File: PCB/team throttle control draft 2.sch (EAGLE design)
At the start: 15 parts, among them IC1 ICL7663CPA, IC4 7805T

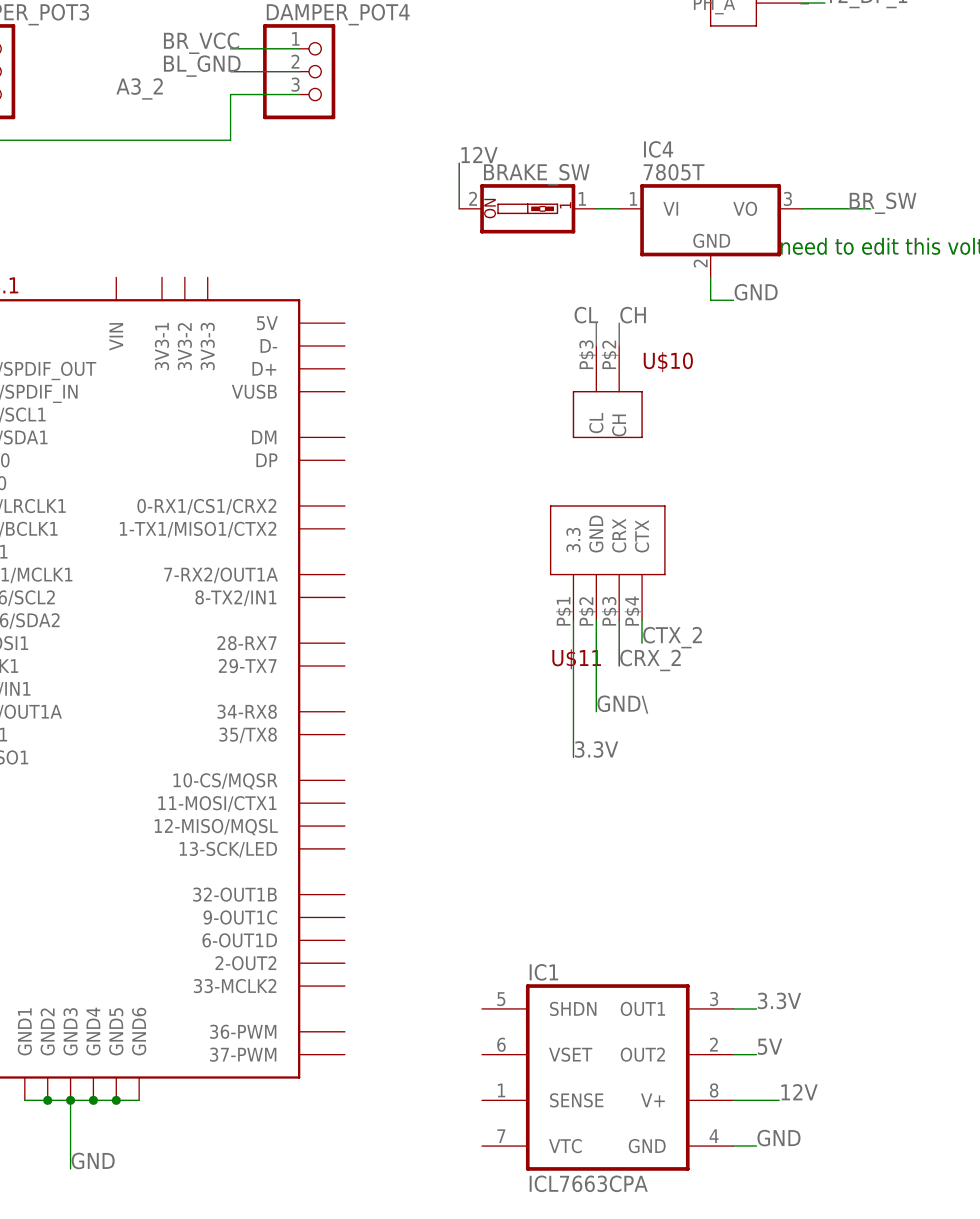
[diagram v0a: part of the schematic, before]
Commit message: Dump car_software's PCB folder into new repository.
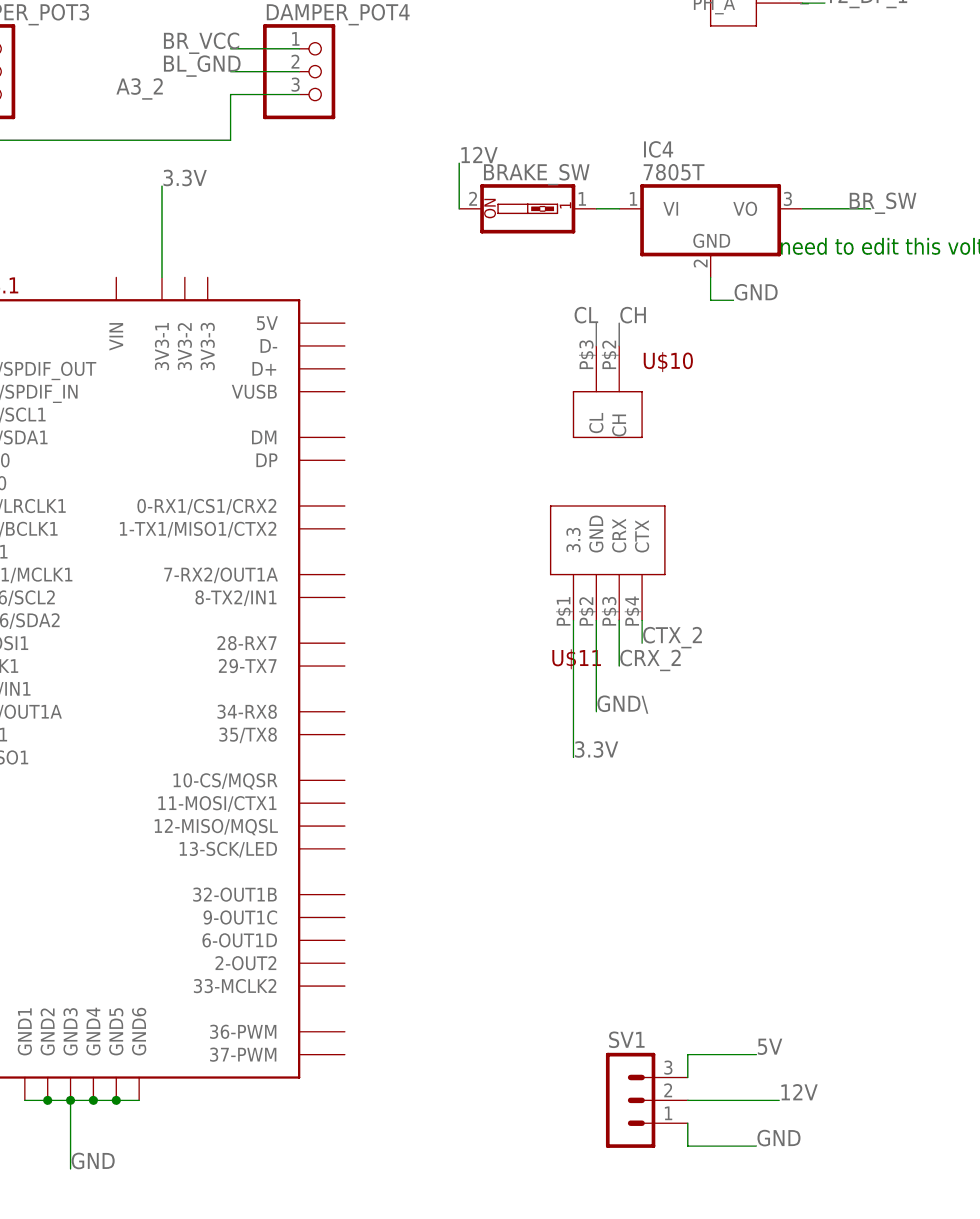
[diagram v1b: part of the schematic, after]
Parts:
- removed IC1: ICL7663CPA, maxim:ICL7663CPA
- added SV1: (no value), con-lstb:MA03-1
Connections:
- net 12V: now also SV1.2; no longer IC1.V+
- net 3.3V: now also U$3.3V3-1; no longer IC1.OUT1
- net 5V: now also SV1.3; no longer IC1.OUT2
- net GND: now also SV1.1; no longer IC1.GND
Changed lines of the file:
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@@
 <?xml version="1.0" encoding="utf-8"?>
 <!DOCTYPE eagle SYSTEM "eagle.dtd">
-<eagle version="7.7.0">
+<eagle version="9.6.2">
 <drawing>
 <settings>
 <setting alwaysvectorfont="no"/>
+<setting keepoldvectorfont="yes"/>
 <setting verticaltext="up"/>
 </settings>
@@
 <layers>
 <layer number="1" name="Top" color="4" fill="1" visible="no" active="no"/>
+<layer number="2" name="Route2" color="1" fill="3" visible="no" active="no"/>
+<layer number="3" name="Route3" color="4" fill="3" visible="no" active="no"/>
+<layer number="4" name="Route4" color="1" fill="4" visible="no" active="no"/>
+<layer number="5" name="Route5" color="4" fill="4" visible="no" active="no"/>
+<layer number="6" name="Route6" color="1" fill="8" visible="no" active="no"/>
+<layer number="7" name="Route7" color="4" fill="8" visible="no" active="no"/>
+<layer number="8" name="Route8" color="1" fill="2" visible="no" active="no"/>
+<layer number="9" name="Route9" color="4" fill="2" visible="no" active="no"/>
+<layer number="10" name="Route10" color="1" fill="7" visible="no" active="no"/>
+<layer number="11" name="Route11" color="4" fill="7" visible="no" active="no"/>
+<layer number="12" name="Route12" color="1" fill="5" visible="no" active="no"/>
+<layer number="13" name="Route13" color="4" fill="5" visible="no" active="no"/>
+<layer number="14" name="Route14" color="1" fill="6" visible="no" active="no"/>
+<layer number="15" name="Route15" color="4" fill="6" visible="no" active="no"/>
 <layer number="16" name="Bottom" color="1" fill="1" visible="no" active="no"/>
 <layer number="17" name="Pads" color="2" fill="1" visible="no" active="no"/>
@@
 <parts>
 <part name="STEERING_ANGLE" library="F-E library custom components" deviceset="ROTARY_ENCODER" device=""/>
-<part name="IC1" library="maxim" deviceset="ICL7663CPA" device=""/>
 <part name="BRAKE_SW" library="special" deviceset="SW_DIP-1" device=""/>
 <part name="DAMPER_POT3" library="adafruit" deviceset="PINHD-1X3" device="CB"/>
@@
 <part name="IC4" library="adafruit" deviceset="78*" device="T" technology="05"/>
 <part name="U$3" library="teensy" deviceset="TEENSY41" device=""/>
+<part name="SV1" library="con-lstb" library_urn="urn:adsk.eagle:library:162" deviceset="MA03-1" device="" package3d_urn="urn:adsk.eagle:package:8339/1"/>
 </parts>
 <sheets>
@@
 <attribute name="NAME" x="129.54" y="147.32" size="1.778" layer="94"/>
 </instance>
-<instance part="IC1" gate="G$1" x="119.38" y="12.7" smashed="yes">
-<attribute name="NAME" x="109.22" y="23.495" size="1.778" layer="95"/>
-<attribute name="VALUE" x="109.22" y="0" size="1.778" layer="96"/>
-</instance>
 <instance part="BRAKE_SW" gate="G$1" x="109.22" y="109.22" smashed="yes">
 <attribute name="NAME" x="104.14" y="112.395" size="1.778" layer="95"/>
@@
 </instance>
 <instance part="U$3" gate="G$1" x="60.96" y="53.34" smashed="yes"/>
+<instance part="SV1" gate="G$1" x="119.38" y="10.16" smashed="yes">
+<attribute name="VALUE" x="118.11" y="2.54" size="1.778" layer="96"/>
+<attribute name="NAME" x="118.11" y="16.002" size="1.778" layer="95"/>
+</instance>
 </instances>
 <busses>
@@
 <net name="GND" class="0">
 <segment>
-<pinref part="IC1" gate="G$1" pin="GND"/>
-<wire x1="132.08" y1="5.08" x2="134.62" y2="5.08" width="0.1524" layer="91"/>
 <label x="134.62" y="5.08" size="1.778" layer="95"/>
+<pinref part="SV1" gate="G$1" pin="1"/>
+<wire x1="134.62" y1="5.08" x2="127" y2="5.08" width="0.1524" layer="91"/>
+<wire x1="127" y1="5.08" x2="127" y2="7.62" width="0.1524" layer="91"/>
 </segment>
 <segment>
@@
 <net name="12V" class="0">
 <segment>
-<pinref part="IC1" gate="G$1" pin="V+"/>
-<wire x1="132.08" y1="10.16" x2="137.16" y2="10.16" width="0.1524" layer="91"/>
 <label x="137.16" y="10.16" size="1.778" layer="95"/>
+<pinref part="SV1" gate="G$1" pin="2"/>
+<wire x1="137.16" y1="10.16" x2="127" y2="10.16" width="0.1524" layer="91"/>
 </segment>
 <segment>
@@
 <net name="3.3V" class="0">
 <segment>
-<pinref part="IC1" gate="G$1" pin="OUT1"/>
-<wire x1="132.08" y1="20.32" x2="134.62" y2="20.32" width="0.1524" layer="91"/>
-<label x="134.62" y="20.32" size="1.778" layer="95"/>
-</segment>
-<segment>
 <pinref part="U$11" gate="G$1" pin="3.3"/>
 <wire x1="114.3" y1="63.5" x2="114.3" y2="48.26" width="0.1524" layer="91"/>
@@
 <label x="83.82" y="175.26" size="1.778" layer="95"/>
 </segment>
+<segment>
+<wire x1="68.58" y1="101.6" x2="68.58" y2="111.76" width="0.1524" layer="91"/>
+<label x="68.58" y="111.76" size="1.778" layer="95"/>
+<pinref part="U$3" gate="G$1" pin="3V3-1"/>
+</segment>
 </net>
 <net name="5V" class="0">
 <segment>
-<pinref part="IC1" gate="G$1" pin="OUT2"/>
-<wire x1="132.08" y1="15.24" x2="134.62" y2="15.24" width="0.1524" layer="91"/>
 <label x="134.62" y="15.24" size="1.778" layer="95"/>
+<pinref part="SV1" gate="G$1" pin="3"/>
+<wire x1="134.62" y1="15.24" x2="127" y2="15.24" width="0.1524" layer="91"/>
+<wire x1="127" y1="15.24" x2="127" y2="12.7" width="0.1524" layer="91"/>
 </segment>
 <segment>
@@
 </schematic>
 </drawing>
+<compatibility>
+<note version="8.2" severity="warning">
+Since Version 8.2, EAGLE supports online libraries. The ids
+of those online libraries will not be understood (or retained)
+with this version.
+</note>
+<note version="8.3" severity="warning">
+Since Version 8.3, EAGLE supports URNs for individual library
+assets (packages, symbols, and devices). The URNs of those assets
+will not be understood (or retained) with this version.
+</note>
+<note version="8.3" severity="warning">
+Since Version 8.3, EAGLE supports the association of 3D packages
+with devices in libraries, schematics, and board files. Those 3D
+packages will not be understood (or retained) with this version.
+</note>
+</compatibility>
 </eagle>
